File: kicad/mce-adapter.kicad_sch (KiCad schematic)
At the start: 19 parts, among them J123 Conn_02x03_Odd_Even, J4 Conn_01x03_Male, SW1 SW_DIP_x03, U1 GAL16V8B

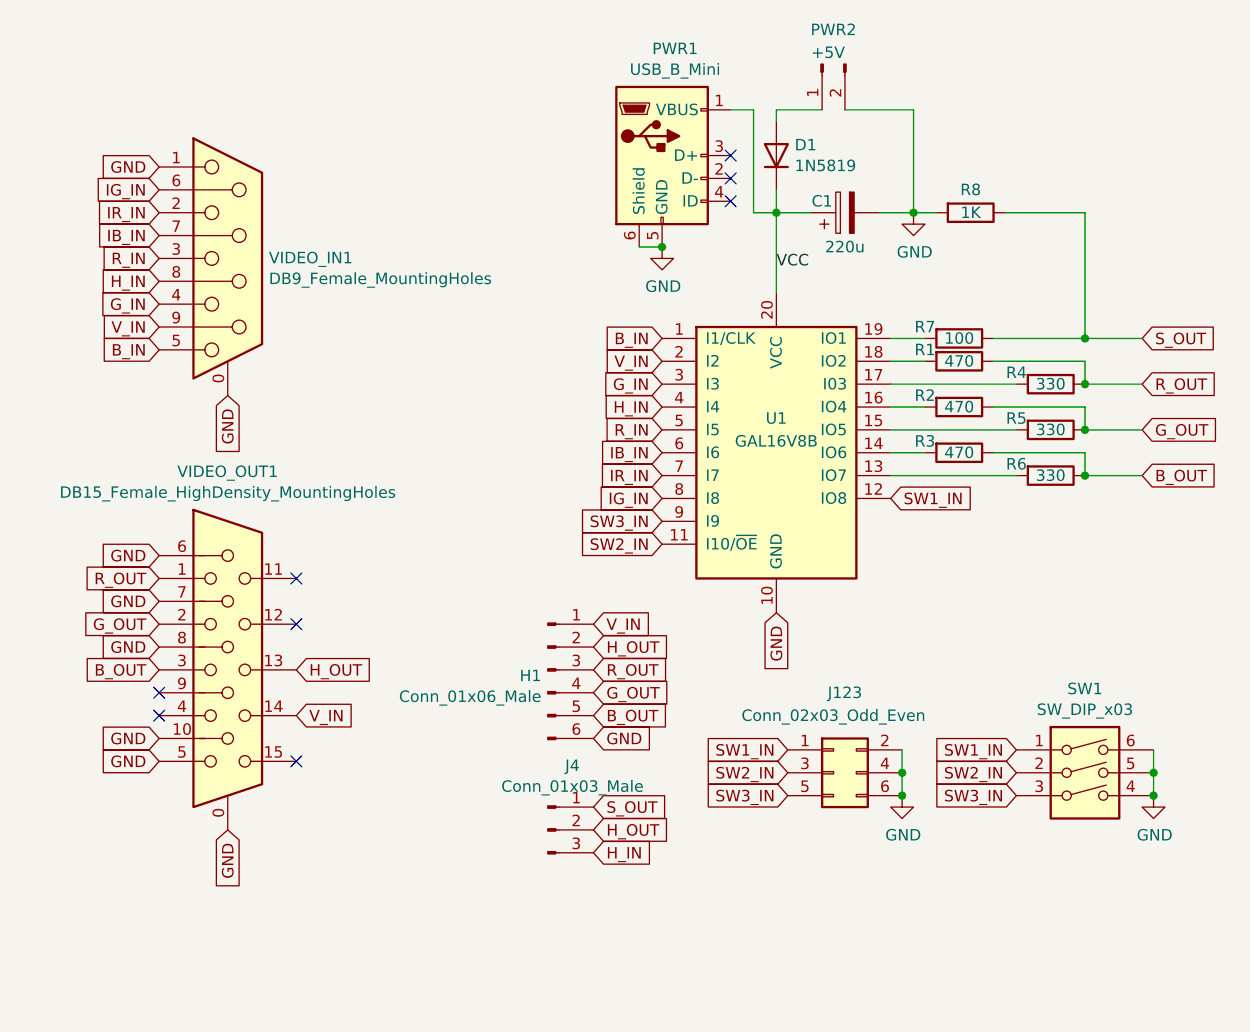
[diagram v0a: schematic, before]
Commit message: Added mode auto-detection
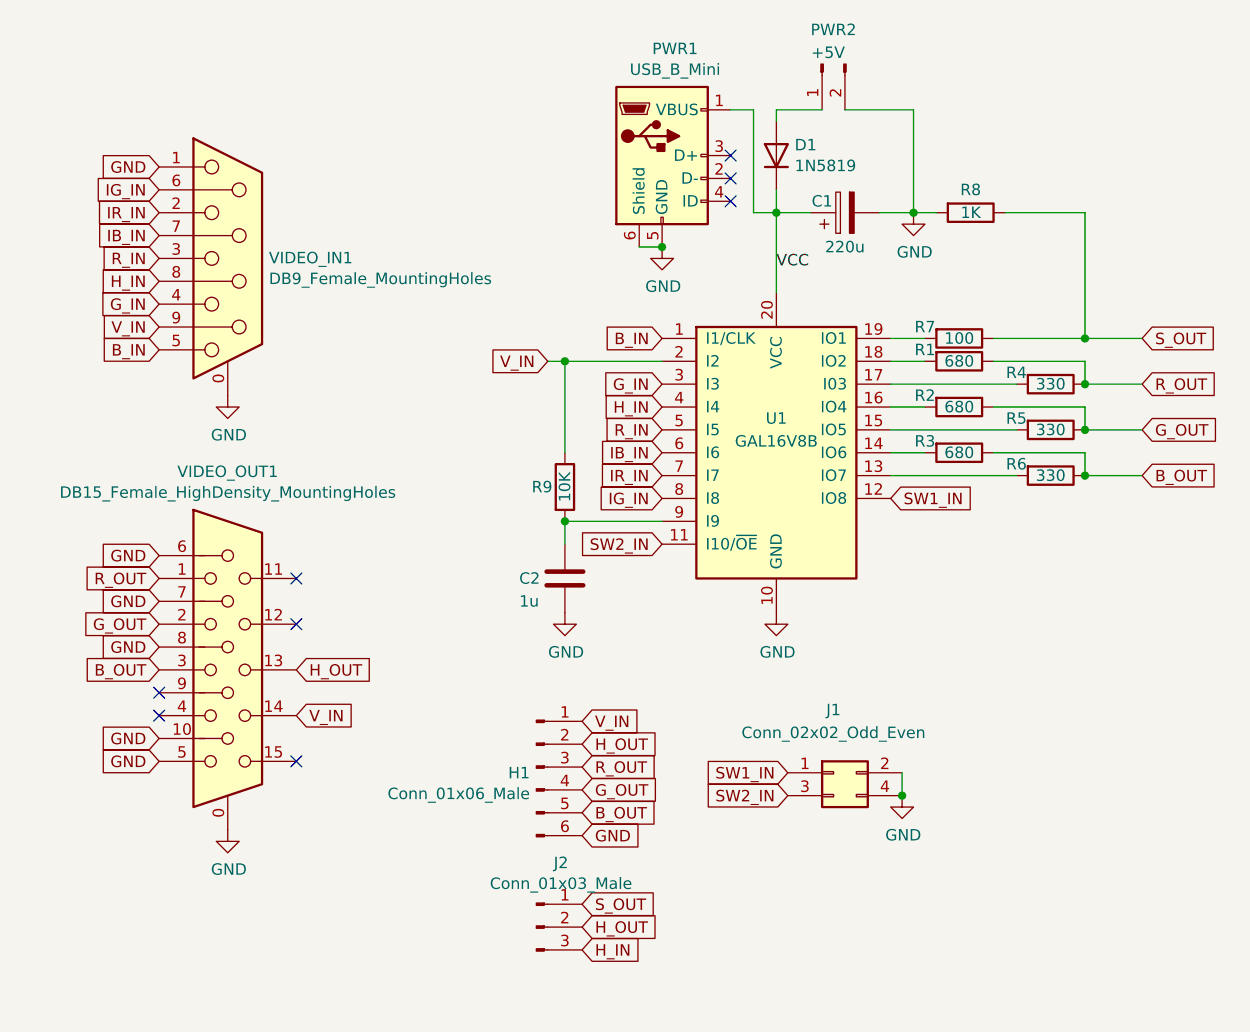
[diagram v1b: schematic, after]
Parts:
- removed SW1: SW_DIP_x03, Button_Switch_THT:SW_DIP_SPSTx03_Slide_9.78x9.8mm_W7.62mm_P2.54mm, symbol Switch:SW_DIP_x03
- added C2: 1u, Capacitor_THT:C_Disc_D5.0mm_W2.5mm_P5.00mm, symbol Device:C
- added R9: 10K, Resistor_THT:R_Axial_DIN0204_L3.6mm_D1.6mm_P7.62mm_Horizontal, symbol Device:R
- J1: renamed from J123; value Conn_02x03_Odd_Even -> Conn_02x02_Odd_Even; footprint Connector_PinHeader_2.54mm:PinHeader_2x03_P2.54mm_Vertical -> Connector_PinHeader_2.54mm:PinHeader_2x02_P2.54mm_Vertical; symbol Connector_Generic:Conn_02x03_Odd_Even -> Connector_Generic:Conn_02x02_Odd_Even
- R1, R2, R3: value 470 -> 680; LCSC C58592 -> C1374269
- renumbered J4 to J2
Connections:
- net GND: now also C2.2; no longer J1.6 (Pin_6)
- net V_IN: now also R9.1
- net SW3_IN: no longer names the net of U1.9 (I9)
- net SW3_IN: now also C2.1, R9.2; no longer J1.5 (Pin_5)
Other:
- moved on the sheet: H1, J2

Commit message: Readjusted resistor networks to get blow 0.7V
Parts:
- removed C1: 220u, Capacitor_THT:CP_Radial_D5.0mm_P2.50mm, symbol Device:CP
- removed R8: 1K, Resistor_THT:R_Axial_DIN0204_L3.6mm_D1.6mm_P7.62mm_Horizontal, symbol Device:R
- added C1: 1u, Capacitor_THT:C_Disc_D5.0mm_W2.5mm_P5.00mm, symbol Device:C
- added R2: 470, Resistor_THT:R_Axial_DIN0204_L3.6mm_D1.6mm_P7.62mm_Horizontal, symbol Device:R
- R1: renamed from R7; value 100 -> 470; LCSC C57438 -> C119317
- R3: renamed from R1; value 680 -> 1.3K; LCSC C1374269 -> C2848597
- R4: value 330 -> 680; LCSC C58608 -> C119320
- R5: renamed from R2; value 680 -> 1.3K; LCSC C1374269 -> C2848597
- R6: renamed from R5; value 330 -> 680; LCSC C58608 -> C119320
- R7: renamed from R3; value 680 -> 1.3K; LCSC C1374269 -> C2848597
- R8: renamed from R6; value 330 -> 680; LCSC C58608 -> C119320
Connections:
- net GND: now also C1.2
- net H_OUT: now also R1.1; no longer J2.2 (Pin_2)
- net S_OUT: now also U1.19 (IO1); no longer R1.1
- net VCC: no longer D1.1 (K), PWR1.1 (VBUS), U1.20 (VCC)
- net V_IN: now also R2.2; no longer H1.1 (Pin_1), VIDEO_OUT1.14
- net at R1.2: now also J2.2 (Pin_2); no longer U1.19 (IO1)
- new net: C1.1, D1.1 (K), PWR1.1 (VBUS), U1.20 (VCC)
- new net V_OUT: H1.1 (Pin_1), R2.1, VIDEO_OUT1.14
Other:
- moved on the sheet: D1, J2, PWR2, R1

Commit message: Update readme and LCSC parts
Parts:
- J1: LCSC C65114 -> C492419
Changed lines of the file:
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@@
       (effects (font (size 1.27 1.27)) hide)
     )
-    (property "LCSC" "C65114" (at 110.49 102.87 0)
+    (property "LCSC" "C492419" (at 110.49 102.87 0)
       (effects (font (size 1.27 1.27)) hide)
     )
